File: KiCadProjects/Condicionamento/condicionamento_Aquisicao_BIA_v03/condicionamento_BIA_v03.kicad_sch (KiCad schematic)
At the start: 35 parts, among them J1 alimentacao analogica, J2 sinais analogicos, J3 comunicacao / sinais digitais, J4 Vref, J5 sinais_condicionados, J6 Eletrodos, J7 alimetacao_Master, U1 AD828AN, U2 BluePill_STM32F103C, U3 BluePill_STM32F103C

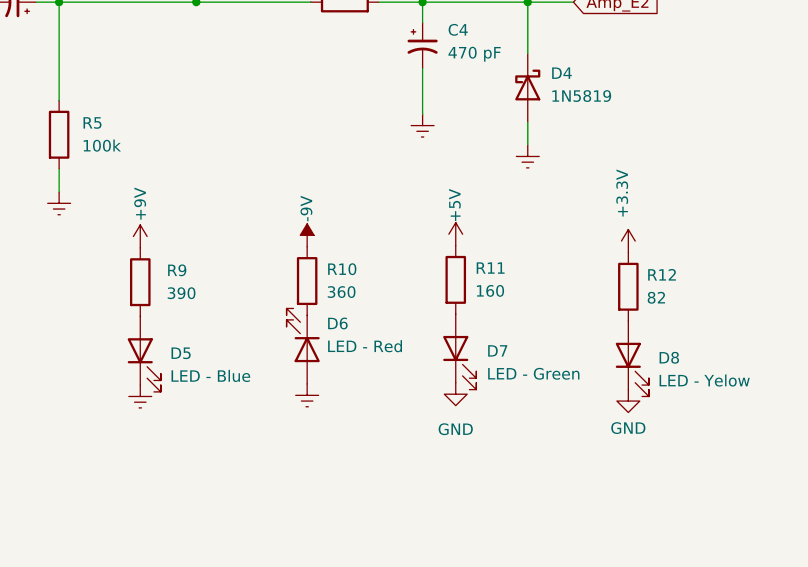
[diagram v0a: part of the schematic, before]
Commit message: Baseado barramento v04 - Finalizado - mudanca valor resitor leds
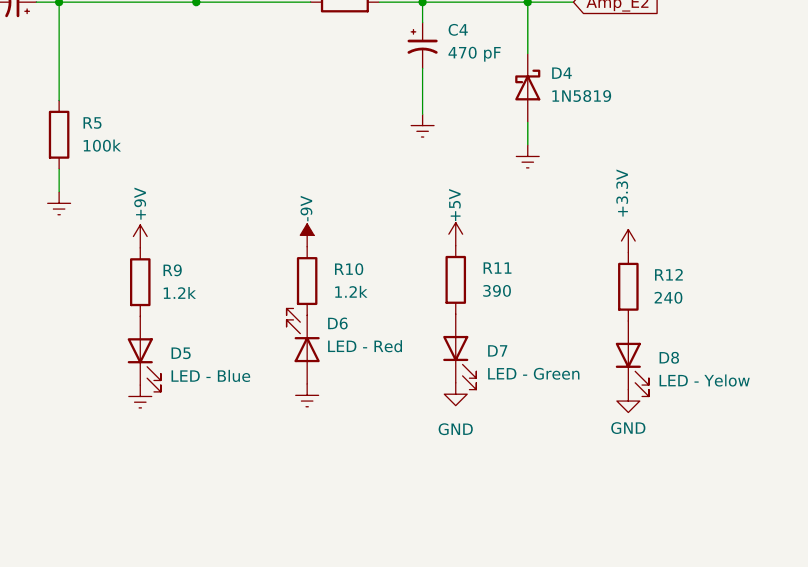
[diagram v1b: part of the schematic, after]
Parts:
- R10: value 360 -> 1.2k
- R11: value 160 -> 390
- R12: value 82 -> 240
- R9: value 390 -> 1.2k
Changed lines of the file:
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@@
   (symbol (lib_id "Device:R") (at 209.677 147.955 0) (unit 1)
     (in_bom yes) (on_board yes) (dnp no) (fields_autoplaced)
-    (property "Reference" "R9" (at 212.598 146.685 0)
-      (effects (font (size 1.27 1.27)) (justify left))
-    )
-    (property "Value" "390" (at 212.598 149.225 0)
+    (property "Reference" "R9" (at 212.09 146.685 0)
+      (effects (font (size 1.27 1.27)) (justify left))
+    )
+    (property "Value" "1.2k" (at 212.09 149.225 0)
       (effects (font (size 1.27 1.27)) (justify left))
     )
@@
   (symbol (lib_id "Device:R") (at 263.906 148.463 0) (unit 1)
     (in_bom yes) (on_board yes) (dnp no) (fields_autoplaced)
-    (property "Reference" "R12" (at 265.938 147.193 0)
-      (effects (font (size 1.27 1.27)) (justify left))
-    )
-    (property "Value" "82" (at 265.938 149.733 0)
+    (property "Reference" "R12" (at 266.7 147.193 0)
+      (effects (font (size 1.27 1.27)) (justify left))
+    )
+    (property "Value" "240" (at 266.7 149.733 0)
       (effects (font (size 1.27 1.27)) (justify left))
     )
@@
   (symbol (lib_id "Device:R") (at 228.219 147.828 0) (unit 1)
     (in_bom yes) (on_board yes) (dnp no) (fields_autoplaced)
-    (property "Reference" "R10" (at 230.378 146.558 0)
-      (effects (font (size 1.27 1.27)) (justify left))
-    )
-    (property "Value" "360" (at 230.378 149.098 0)
+    (property "Reference" "R10" (at 231.14 146.558 0)
+      (effects (font (size 1.27 1.27)) (justify left))
+    )
+    (property "Value" "1.2k" (at 231.14 149.098 0)
       (effects (font (size 1.27 1.27)) (justify left))
     )
@@
   (symbol (lib_id "Device:R") (at 244.729 147.701 0) (unit 1)
     (in_bom yes) (on_board yes) (dnp no) (fields_autoplaced)
-    (property "Reference" "R11" (at 246.888 146.431 0)
-      (effects (font (size 1.27 1.27)) (justify left))
-    )
-    (property "Value" "160" (at 246.888 148.971 0)
-      (effects (font (size 1.27 1.27)) (justify left))
-    )
+    (property "Reference" "R11" (at 247.65 146.431 0)
+      (effects (font (size 1.27 1.27)) (justify left))
+    )
+    (property "Value" "390" (at 247.65 148.971 0)
+      (effects (font (size 1.27 1.27)) (justify left))
+    )

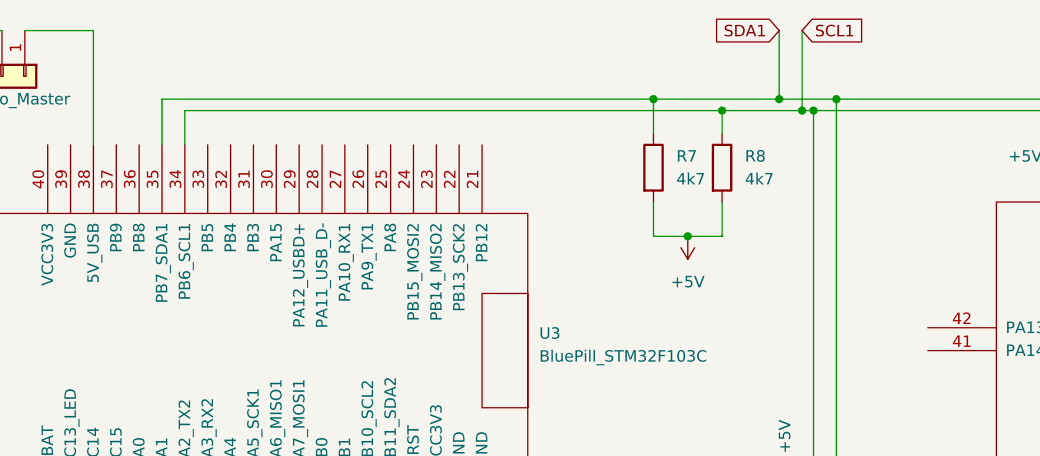
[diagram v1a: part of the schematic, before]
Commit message: Baseado barramento v04 - Finalizado - remocao resistor pullup i2c
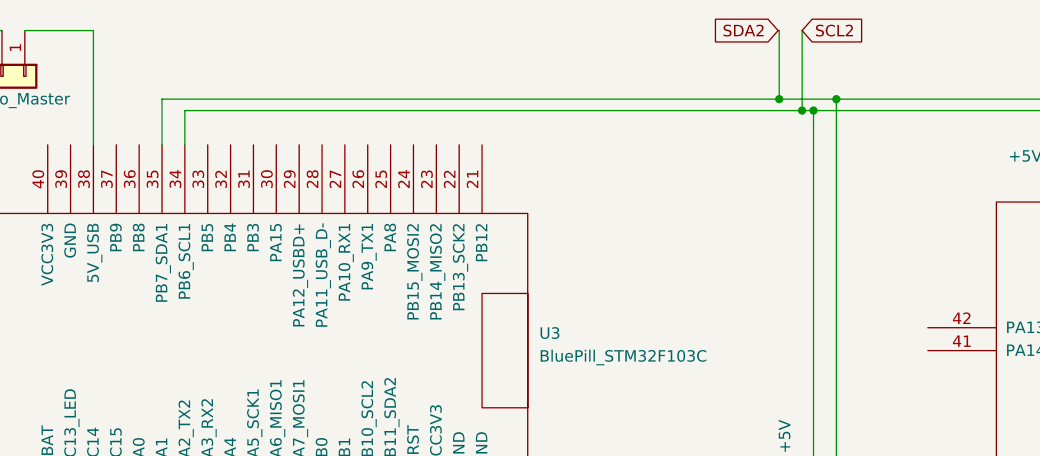
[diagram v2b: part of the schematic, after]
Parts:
- removed R7, R8: 4k7, Resistor_THT:R_Axial_DIN0207_L6.3mm_D2.5mm_P7.62mm_Horizontal, symbol Device:R
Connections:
- net SCL1: no longer Brd1.3 (SCL), U2.34 (PB6_SCL1), U3.34 (PB6_SCL1)
- net SCL2: now also Brd1.3 (SCL), U2.34 (PB6_SCL1), U3.34 (PB6_SCL1)
- net SDA1: no longer Brd1.4 (SDA), U2.35 (PB7_SDA1), U3.35 (PB7_SDA1)
- net SDA2: now also Brd1.4 (SDA), U2.35 (PB7_SDA1), U3.35 (PB7_SDA1)
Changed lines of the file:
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@@
   (junction (at 153.67 22.86) (diameter 0) (color 0 0 0 0)
   )
-  (junction (at 144.78 22.86) (diameter 0) (color 0 0 0 0)
-  )
-  (junction (at 137.16 21.59) (diameter 0) (color 0 0 0 0)
-  )
   (junction (at 215.9 116.84) (diameter 0) (color 0 0 0 0)
   )
@@
   (junction (at 151.13 21.59) (diameter 0) (color 0 0 0 0)
   )
-  (junction (at 140.97 36.83) (diameter 0) (color 0 0 0 0)
-  )
   (junction (at 129.54 113.03) (diameter 0) (color 0 0 0 0)
   )
@@
     (stroke (width 0) (type default))
   )
-  (wire (pts (xy 144.78 33.02) (xy 144.78 36.83))
-    (stroke (width 0) (type default))
-  )
   (wire (pts (xy 77.47 113.03) (xy 64.77 113.03))
     (stroke (width 0) (type default))
@@
     (stroke (width 0) (type default))
   )
-  (wire (pts (xy 137.16 21.59) (xy 82.55 21.59))
+  (wire (pts (xy 82.55 21.59) (xy 151.13 21.59))
     (stroke (width 0) (type default))
   )
@@
     (stroke (width 0) (type default))
   )
-  (wire (pts (xy 144.78 36.83) (xy 140.97 36.83))
-    (stroke (width 0) (type default))
-  )
   (wire (pts (xy 252.73 130.175) (xy 252.73 132.715))
     (stroke (width 0) (type default))
@@
     (stroke (width 0) (type default))
   )
-  (wire (pts (xy 144.78 22.86) (xy 144.78 25.4))
-    (stroke (width 0) (type default))
-  )
   (wire (pts (xy 170.18 114.3) (xy 170.18 116.84))
     (stroke (width 0) (type default))
@@
     (stroke (width 0) (type default))
   )
-  (wire (pts (xy 137.16 33.02) (xy 137.16 36.83))
-    (stroke (width 0) (type default))
-  )
   (wire (pts (xy 104.013 178.181) (xy 104.013 184.785))
     (stroke (width 0) (type default))
@@
     (stroke (width 0) (type default))
   )
-  (wire (pts (xy 85.09 22.86) (xy 144.78 22.86))
+  (wire (pts (xy 85.09 22.86) (xy 153.67 22.86))
     (stroke (width 0) (type default))
   )
@@
     (stroke (width 0) (type default))
   )
-  (wire (pts (xy 151.13 21.59) (xy 137.16 21.59))
-    (stroke (width 0) (type default))
-  )
   (wire (pts (xy 213.36 22.86) (xy 213.36 25.4))
     (stroke (width 0) (type default))
@@
     (stroke (width 0) (type default))
   )
-  (wire (pts (xy 144.78 22.86) (xy 153.67 22.86))
-    (stroke (width 0) (type default))
-  )
   (wire (pts (xy 69.342 177.419) (xy 73.152 177.419))
     (stroke (width 0) (type default))
@@
     (stroke (width 0) (type default))
   )
-  (wire (pts (xy 137.16 36.83) (xy 140.97 36.83))
+  (wire (pts (xy 151.003 13.97) (xy 151.13 13.97))
     (stroke (width 0) (type default))
   )
@@
   )
   (wire (pts (xy 70.104 155.829) (xy 65.024 155.829))
-    (stroke (width 0) (type default))
-  )
-  (wire (pts (xy 137.16 21.59) (xy 137.16 25.4))
     (stroke (width 0) (type default))
   )
@@
     )
   )
-  (global_label "SDA1" (shape input) (at 151.13 13.97 180) (fields_autoplaced)
-    (effects (font (size 1.27 1.27)) (justify right))
-    (property "Intersheetrefs" "${INTERSHEET_REFS}" (at 143.4466 13.97 0)
-      (effects (font (size 1.27 1.27)) (justify right) hide)
-    )
-  )
   (global_label "SCL1" (shape input) (at 93.853 184.785 90) (fields_autoplaced)
     (effects (font (size 1.27 1.27)) (justify left))
@@
     )
   )
+  (global_label "SDA2" (shape input) (at 151.003 13.97 180) (fields_autoplaced)
+    (effects (font (size 1.27 1.27)) (justify right))
+    (property "Intersheetrefs" "${INTERSHEET_REFS}" (at 143.2402 13.97 0)
+      (effects (font (size 1.27 1.27)) (justify right) hide)
+    )
+  )
   (global_label "I2" (shape input) (at 47.752 184.15 90) (fields_autoplaced)
     (effects (font (size 1.27 1.27)) (justify left))
     (property "Intersheetrefs" "${INTERSHEET_REFS}" (at 47.752 179.4299 90)
+      (effects (font (size 1.27 1.27)) (justify left) hide)
+    )
+  )
+  (global_label "SCL2" (shape input) (at 153.67 13.97 0) (fields_autoplaced)
+    (effects (font (size 1.27 1.27)) (justify left))
+    (property "Intersheetrefs" "${INTERSHEET_REFS}" (at 161.3723 13.97 0)
       (effects (font (size 1.27 1.27)) (justify left) hide)
     )
@@
     (property "Intersheetrefs" "${INTERSHEET_REFS}" (at 70.9773 101.6 0)
       (effects (font (size 1.27 1.27)) (justify right) hide)
-    )
-  )
-  (global_label "SCL1" (shape input) (at 153.67 13.97 0) (fields_autoplaced)
-    (effects (font (size 1.27 1.27)) (justify left))
-    (property "Intersheetrefs" "${INTERSHEET_REFS}" (at 161.2929 13.97 0)
-      (effects (font (size 1.27 1.27)) (justify left) hide)
     )
   )
@@
     )
   )
-  (symbol (lib_id "power:+5V") (at 140.97 36.83 180) (unit 1)
-    (in_bom yes) (on_board yes) (dnp no) (fields_autoplaced)
-    (property "Reference" "#PWR01" (at 140.97 33.02 0)
-      (effects (font (size 1.27 1.27)) hide)
-    )
-    (property "Value" "+5V" (at 140.97 41.91 0)
-      (effects (font (size 1.27 1.27)))
-    )
-    (property "Footprint" "" (at 140.97 36.83 0)
-      (effects (font (size 1.27 1.27)) hide)
-    )
-    (property "Datasheet" "" (at 140.97 36.83 0)
-      (effects (font (size 1.27 1.27)) hide)
-    )
-    (pin "1")
-    (instances
-      (project "condicionamento_BIA_v03"
-        (path "/f0ff92cf-26e5-4ab9-977d-5f9689e8a5d0"
-          (reference "#PWR01") (unit 1)
-        )
-      )
-    )
-  )
   (symbol (lib_id "Device:R") (at 92.71 101.6 0) (mirror y) (unit 1)
     (in_bom yes) (on_board yes) (dnp no) (fields_autoplaced)
@@
         (path "/f0ff92cf-26e5-4ab9-977d-5f9689e8a5d0"
           (reference "R4") (unit 1)
-        )
-      )
-    )
-  )
-  (symbol (lib_id "Device:R") (at 144.78 29.21 0) (unit 1)
-    (in_bom yes) (on_board yes) (dnp no) (fields_autoplaced)
-    (property "Reference" "R8" (at 147.32 27.94 0)
-      (effects (font (size 1.27 1.27)) (justify left))
-    )
-    (property "Value" "4k7" (at 147.32 30.48 0)
-      (effects (font (size 1.27 1.27)) (justify left))
-    )
-    (property "Footprint" "Resistor_THT:R_Axial_DIN0207_L6.3mm_D2.5mm_P7.62mm_Horizontal" (at 143.002 29.21 90)
-      (effects (font (size 1.27 1.27)) hide)
-    )
-    (property "Datasheet" "~" (at 144.78 29.21 0)
-      (effects (font (size 1.27 1.27)) hide)
-    )
-    (pin "1")
-    (pin "2")
-    (instances
-      (project "condicionamento_BIA_v03"
-        (path "/f0ff92cf-26e5-4ab9-977d-5f9689e8a5d0"
-          (reference "R8") (unit 1)
         )
       )
@@
         )
       )
-    )
-  )
-  (symbol (lib_id "Device:R") (at 137.16 29.21 0) (unit 1)
-    (in_bom yes) (on_board yes) (dnp no) (fields_autoplaced)
-    (property "Reference" "R7" (at 139.7 27.94 0)
-      (effects (font (size 1.27 1.27)) (justify left))
-    )
-    (property "Value" "4k7" (at 139.7 30.48 0)
-      (effects (font (size 1.27 1.27)) (justify left))
-    )
-    (property "Footprint" "Resistor_THT:R_Axial_DIN0207_L6.3mm_D2.5mm_P7.62mm_Horizontal" (at 135.382 29.21 90)
-      (effects (font (size 1.27 1.27)) hide)
-    )
-    (property "Datasheet" "~" (at 137.16 29.21 0)
-      (effects (font (size 1.27 1.27)) hide)
-    )
-    (pin "1")
-    (pin "2")
-    (instances
-      (project "condicionamento_BIA_v03"
-        (path "/f0ff92cf-26e5-4ab9-977d-5f9689e8a5d0"
-          (reference "R7") (unit 1)
-        )
-      )
